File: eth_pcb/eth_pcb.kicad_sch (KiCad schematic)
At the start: 0 parts

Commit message: added components to library and built crystal circuit
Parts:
- added U1: W5500, W5500:QFP50P900X900X160-48N, symbol eth_pcb:W5500
- added Y1: crystal, ABLS-25.000MHZ-B2F-T:XTAL_ABLS-25.000MHZ-B2F-T, symbol eth_pcb:crystal

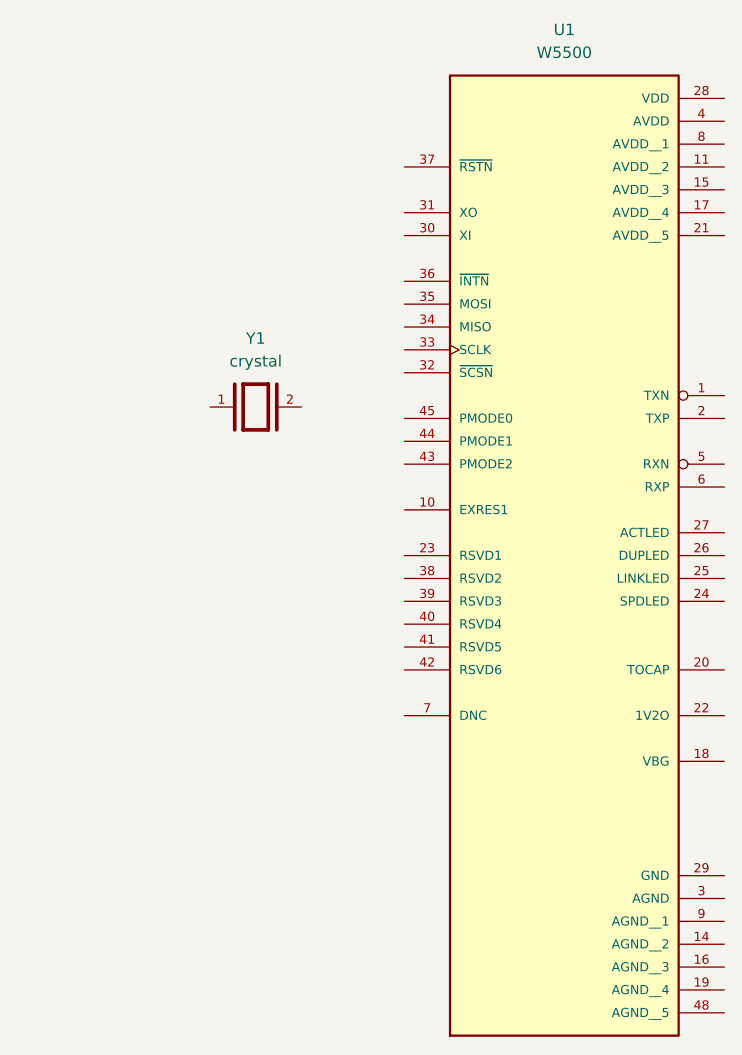
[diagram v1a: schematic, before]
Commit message: added components to library and built crystal circuit
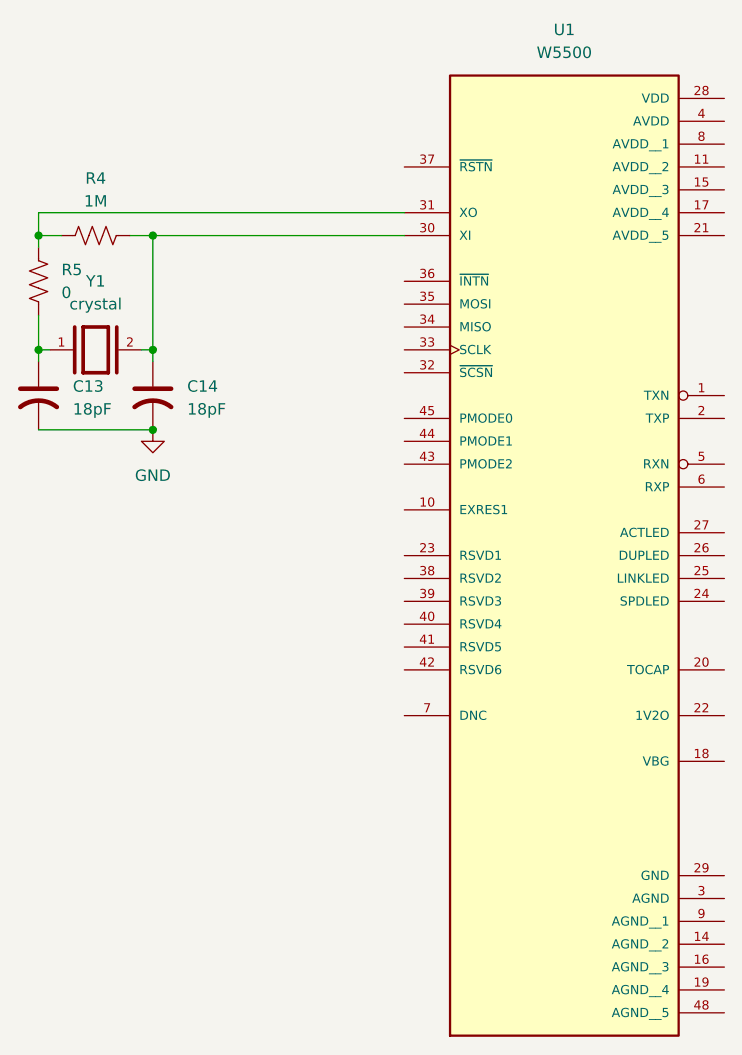
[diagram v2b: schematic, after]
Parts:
- added C13, C14: 18pF, symbol Device:C_US
- added R4: 1M, symbol Device:R_US
- added R5: 0, symbol Device:R_US
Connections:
- net at U1.30 (XI): now also Y1.2, C14.1, R4.2
- net at U1.31 (XO): now also R4.1, R5.2
- net at Y1.1: now also C13.1, R5.1
- new net GND: C13.2, C14.2
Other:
- moved on the sheet: Y1
